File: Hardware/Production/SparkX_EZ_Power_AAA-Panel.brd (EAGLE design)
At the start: 187.2 x 136.7 mm, 1386 parts, among them J10 AVR_SPI_PROG_3X2TESTPOINTS, J12 AVR_SPI_PROG_3X2TESTPOINTS, J14 AVR_SPI_PROG_3X2TESTPOINTS, J16 AVR_SPI_PROG_3X2TESTPOINTS, J18 AVR_SPI_PROG_3X2TESTPOINTS, J20 AVR_SPI_PROG_3X2TESTPOINTS, J22 AVR_SPI_PROG_3X2TESTPOINTS, J24 AVR_SPI_PROG_3X2TESTPOINTS, J26 AVR_SPI_PROG_3X2TESTPOINTS, J28 AVR_SPI_PROG_3X2TESTPOINTS, J3 AVR_SPI_PROG_3X2TESTPOINTS, J30 AVR_SPI_PROG_3X2TESTPOINTS, J32 AVR_SPI_PROG_3X2TESTPOINTS, J34 AVR_SPI_PROG_3X2TESTPOINTS, J36 AVR_SPI_PROG_3X2TESTPOINTS, J38 AVR_SPI_PROG_3X2TESTPOINTS, J4 AVR_SPI_PROG_3X2TESTPOINTS, J40 AVR_SPI_PROG_3X2TESTPOINTS, J42 AVR_SPI_PROG_3X2TESTPOINTS, J44 AVR_SPI_PROG_3X2TESTPOINTS, J46 AVR_SPI_PROG_3X2TESTPOINTS, J48 AVR_SPI_PROG_3X2TESTPOINTS, J50 AVR_SPI_PROG_3X2TESTPOINTS, J52 AVR_SPI_PROG_3X2TESTPOINTS, J54 AVR_SPI_PROG_3X2TESTPOINTS, J56 AVR_SPI_PROG_3X2TESTPOINTS, J58 AVR_SPI_PROG_3X2TESTPOINTS, J6 AVR_SPI_PROG_3X2TESTPOINTS, J60 AVR_SPI_PROG_3X2TESTPOINTS, J8 AVR_SPI_PROG_3X2TESTPOINTS, U1 ATTINY43_QFN20, U10 TPS61200, U11 ATTINY43_QFN20, U12 TPS61200, U13 ATTINY43_QFN20, U14 TPS61200, U15 ATTINY43_QFN20, U16 TPS61200, U17 ATTINY43_QFN20, U18 TPS61200, U19 ATTINY43_QFN20, U2 TPS61200, U20 TPS61200, U21 ATTINY43_QFN20, U22 TPS61200, U23 ATTINY43_QFN20, U24 TPS61200, U25 ATTINY43_QFN20, U26 TPS61200, U27 ATTINY43_QFN20, U28 TPS61200, U29 ATTINY43_QFN20, U3 ATTINY43_QFN20, U30 TPS61200, U31 ATTINY43_QFN20, U32 TPS61200, U33 ATTINY43_QFN20, U34 TPS61200, U35 ATTINY43_QFN20, U36 TPS61200, U37 ATTINY43_QFN20, U38 TPS61200, U39 ATTINY43_QFN20, U4 TPS61200, U40 TPS61200, U41 ATTINY43_QFN20, U42 TPS61200, U43 ATTINY43_QFN20, U44 TPS61200, U45 ATTINY43_QFN20, U46 TPS61200, U47 ATTINY43_QFN20, U48 TPS61200, U49 ATTINY43_QFN20, U5 ATTINY43_QFN20, U50 TPS61200, U51 ATTINY43_QFN20, U52 TPS61200, U53 ATTINY43_QFN20, U54 TPS61200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

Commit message: Final tweaks
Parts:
- added U$391, U$405, U$419: (no value), output:5#5V0
- added U$392, U$406, U$420: (no value), output:MAX0
- added U$393, U$395, U$407, U$409: SPARKX-LOGO3, SparkX:SPARKX-SMALL
- added U$394, U$408: (no value), output:#OUT#0
- added U$396, U$410: (no value), output:#IN#0
- added U$397, U$411: (no value), output:#VIN#0
- added U$398, U$412: (no value), output:#3V3_EN#0
- added U$399, U$413: (no value), output:#PROC_PWR#0
- added U$400, U$414: (no value), output:#AT_VCC#0
- added U$401, U$402, U$415, U$416: (no value), output:EZ_POWER_AAA0
- added U$403, U$417: (no value), output:#TXD#0
- added U$404, U$418: (no value), output:#RXD#0
- U$10, U$195, U$377: device output:5#5V_MAX0 -> output:5#5V0
- U$100, U$114, U$282, U$296: device output:EZ_POWER_AAA0 -> output:#OUT#0
- U$101, U$113, U$127, U$269, U$283, U$295, U$309, U$87: value (none) -> SPARKX-LOGO3; device output:EZ_POWER_AAA0 -> SparkX:SPARKX-SMALL
- U$102, U$284: device output:#TXD#0 -> output:#IN#0
- U$103, U$285: device output:#RXD#0 -> output:#VIN#0
- U$104, U$286: device output:5#5V_MAX0 -> output:#3V3_EN#0
- U$105, U$133, U$287, U$315: value SPARKX-LOGO3 -> (none); device SparkX:SPARKX-SMALL -> output:#PROC_PWR#0
- U$106, U$288: device output:#OUT#0 -> output:#AT_VCC#0
- U$107, U$248, U$261, U$276, U$289, U$66, U$79, U$94: value SPARKX-LOGO3 -> (none); device SparkX:SPARKX-SMALL -> output:EZ_POWER_AAA0
- U$108, U$121, U$290, U$303: device output:#IN#0 -> output:EZ_POWER_AAA0
- U$109, U$291: device output:#VIN#0 -> output:#TXD#0
- U$11, U$196, U$224, U$378, U$42: value SPARKX-LOGO3 -> (none); device SparkX:SPARKX-SMALL -> output:MAX0
- U$110, U$292: device output:#3V3_EN#0 -> output:#RXD#0
- U$111, U$293: device output:#PROC_PWR#0 -> output:5#5V0
- U$112, U$294: device output:#AT_VCC#0 -> output:MAX0
- U$115, U$141, U$297, U$323: value (none) -> SPARKX-LOGO3; device output:#TXD#0 -> SparkX:SPARKX-SMALL
- U$116, U$298: device output:#RXD#0 -> output:#IN#0
- U$117, U$299: device output:5#5V_MAX0 -> output:#VIN#0
- U$118, U$146, U$300, U$328: value SPARKX-LOGO3 -> (none); device SparkX:SPARKX-SMALL -> output:#3V3_EN#0
- U$119, U$301: device output:#OUT#0 -> output:#PROC_PWR#0
- U$120, U$274, U$302, U$92: value SPARKX-LOGO3 -> (none); device SparkX:SPARKX-SMALL -> output:#AT_VCC#0
- U$122, U$135, U$304, U$317: device output:#VIN#0 -> output:EZ_POWER_AAA0
- U$123, U$305: device output:#3V3_EN#0 -> output:#TXD#0
- U$124, U$306: device output:#PROC_PWR#0 -> output:#RXD#0
- U$125, U$307: device output:#AT_VCC#0 -> output:5#5V0
- U$126, U$140, U$308, U$322: device output:EZ_POWER_AAA0 -> output:MAX0
- U$128, U$310: device output:#TXD#0 -> output:#OUT#0
- U$129, U$155, U$311, U$337: value (none) -> SPARKX-LOGO3; device output:#RXD#0 -> SparkX:SPARKX-SMALL
- U$130, U$312: device output:5#5V_MAX0 -> output:#IN#0
- U$131, U$159, U$313, U$341: value SPARKX-LOGO3 -> (none); device SparkX:SPARKX-SMALL -> output:#VIN#0
- U$132, U$314: device output:#OUT#0 -> output:#3V3_EN#0
- U$134, U$316: device output:#IN#0 -> output:#AT_VCC#0
- U$136, U$149, U$318, U$331: device output:#3V3_EN#0 -> output:EZ_POWER_AAA0
- U$137, U$319: device output:#PROC_PWR#0 -> output:#TXD#0
- U$138, U$320: device output:#AT_VCC#0 -> output:#RXD#0
- U$139, U$153, U$321, U$335: device output:EZ_POWER_AAA0 -> output:5#5V0
- U$14, U$171, U$197, U$353, U$379: value (none) -> SPARKX-LOGO3; device output:#OUT#0 -> SparkX:SPARKX-SMALL
- U$142, U$324: device output:#RXD#0 -> output:#OUT#0
- U$143, U$169, U$325, U$351: value (none) -> SPARKX-LOGO3; device output:5#5V_MAX0 -> SparkX:SPARKX-SMALL
- U$144, U$172, U$326, U$354: value SPARKX-LOGO3 -> (none); device SparkX:SPARKX-SMALL -> output:#IN#0
- U$145, U$327: device output:#OUT#0 -> output:#VIN#0
- U$147, U$329: device output:#IN#0 -> output:#PROC_PWR#0
- U$148, U$330: device output:#VIN#0 -> output:#AT_VCC#0
- U$15, U$170, U$198, U$352, U$380: value SPARKX-LOGO3 -> (none); device SparkX:SPARKX-SMALL -> output:#OUT#0
- U$150, U$163, U$332, U$345: device output:#PROC_PWR#0 -> output:EZ_POWER_AAA0
- U$151, U$333: device output:#AT_VCC#0 -> output:#TXD#0
- U$152, U$166, U$334, U$348: device output:EZ_POWER_AAA0 -> output:#RXD#0
- U$154, U$336: device output:#TXD#0 -> output:MAX0
- U$156, U$338: device output:5#5V_MAX0 -> output:#OUT#0
- U$158, U$340: device output:#OUT#0 -> output:#IN#0
- U$16, U$199, U$225, U$381, U$43: value (none) -> SPARKX-LOGO3; device output:#IN#0 -> SparkX:SPARKX-SMALL
- U$160, U$342: device output:#IN#0 -> output:#3V3_EN#0
- U$161, U$343: device output:#VIN#0 -> output:#PROC_PWR#0
- U$162, U$344: device output:#3V3_EN#0 -> output:#AT_VCC#0
- U$164, U$177, U$346, U$359: device output:#AT_VCC#0 -> output:EZ_POWER_AAA0
- U$165, U$179, U$347, U$361: device output:EZ_POWER_AAA0 -> output:#TXD#0
- U$167, U$349: device output:#TXD#0 -> output:5#5V0
- U$168, U$350: device output:#RXD#0 -> output:MAX0
- U$17, U$200, U$382: device output:#VIN#0 -> output:#IN#0
- U$173, U$355: device output:#IN#0 -> output:#VIN#0
- U$174, U$356: device output:#VIN#0 -> output:#3V3_EN#0
- U$175, U$357: device output:#3V3_EN#0 -> output:#PROC_PWR#0
- U$176, U$358: device output:#PROC_PWR#0 -> output:#AT_VCC#0
- U$18, U$201, U$383: device output:#3V3_EN#0 -> output:#VIN#0
- U$180, U$362: device output:#TXD#0 -> output:#RXD#0
- U$181, U$363: device output:#RXD#0 -> output:5#5V0
- U$182, U$364: device output:5#5V_MAX0 -> output:MAX0
- U$19, U$202, U$384: device output:#PROC_PWR#0 -> output:#3V3_EN#0
- U$203, U$21, U$385: device output:#AT_VCC#0 -> output:#PROC_PWR#0
- U$204, U$218, U$22, U$36, U$386: device output:EZ_POWER_AAA0 -> output:#AT_VCC#0
- U$206, U$219, U$24, U$37, U$388: device output:#TXD#0 -> output:EZ_POWER_AAA0
- U$207, U$25, U$389: device output:#RXD#0 -> output:#TXD#0
- U$208, U$26, U$390: device output:5#5V_MAX0 -> output:#RXD#0
- U$209, U$237, U$27, U$55: value SPARKX-LOGO3 -> (none); device SparkX:SPARKX-SMALL -> output:5#5V0
- U$210, U$28: device output:#OUT#0 -> output:MAX0
- U$212, U$30: device output:#IN#0 -> output:#OUT#0
- U$213, U$239, U$31, U$57: value (none) -> SPARKX-LOGO3; device output:#VIN#0 -> SparkX:SPARKX-SMALL
- U$214, U$32: device output:#3V3_EN#0 -> output:#IN#0
- U$215, U$33: device output:#PROC_PWR#0 -> output:#VIN#0
- U$216, U$34: device output:#AT_VCC#0 -> output:#3V3_EN#0
- U$217, U$231, U$35, U$49: device output:EZ_POWER_AAA0 -> output:#PROC_PWR#0
- U$220, U$233, U$38, U$51: device output:#RXD#0 -> output:EZ_POWER_AAA0
- U$221, U$39: device output:5#5V_MAX0 -> output:#TXD#0
- U$222, U$250, U$40, U$68: value SPARKX-LOGO3 -> (none); device SparkX:SPARKX-SMALL -> output:#RXD#0
- U$223, U$41: device output:#OUT#0 -> output:5#5V0
- U$226, U$44: device output:#VIN#0 -> output:#OUT#0
- U$227, U$253, U$45, U$71: value (none) -> SPARKX-LOGO3; device output:#3V3_EN#0 -> SparkX:SPARKX-SMALL
- U$228, U$46: device output:#PROC_PWR#0 -> output:#IN#0
- U$229, U$47: device output:#AT_VCC#0 -> output:#VIN#0
- U$230, U$244, U$48, U$62: device output:EZ_POWER_AAA0 -> output:#3V3_EN#0
- U$232, U$50: device output:#TXD#0 -> output:#AT_VCC#0
- U$234, U$247, U$52, U$65: device output:5#5V_MAX0 -> output:EZ_POWER_AAA0
- U$235, U$263, U$53, U$81: value SPARKX-LOGO3 -> (none); device SparkX:SPARKX-SMALL -> output:#TXD#0
- U$236, U$54: device output:#OUT#0 -> output:#RXD#0
- U$238, U$56: device output:#IN#0 -> output:MAX0
- U$240, U$58: device output:#3V3_EN#0 -> output:#OUT#0
- U$241, U$267, U$59, U$85: value (none) -> SPARKX-LOGO3; device output:#PROC_PWR#0 -> SparkX:SPARKX-SMALL
- U$242, U$60: device output:#AT_VCC#0 -> output:#IN#0
- U$243, U$257, U$61, U$75: device output:EZ_POWER_AAA0 -> output:#VIN#0
- U$245, U$63: device output:#TXD#0 -> output:#PROC_PWR#0
- U$246, U$64: device output:#RXD#0 -> output:#AT_VCC#0
- U$249, U$67: device output:#OUT#0 -> output:#TXD#0
- U$251, U$69: device output:#IN#0 -> output:5#5V0
- U$252, U$70: device output:#VIN#0 -> output:MAX0
- U$254, U$72: device output:#PROC_PWR#0 -> output:#OUT#0
- U$255, U$281, U$73, U$99: value (none) -> SPARKX-LOGO3; device output:#AT_VCC#0 -> SparkX:SPARKX-SMALL
- U$256, U$270, U$74, U$88: device output:EZ_POWER_AAA0 -> output:#IN#0
- U$258, U$76: device output:#TXD#0 -> output:#3V3_EN#0
- U$259, U$77: device output:#RXD#0 -> output:#PROC_PWR#0
- U$260, U$78: device output:5#5V_MAX0 -> output:#AT_VCC#0
- U$262, U$275, U$80, U$93: device output:#OUT#0 -> output:EZ_POWER_AAA0
- U$264, U$82: device output:#IN#0 -> output:#RXD#0
- U$265, U$83: device output:#VIN#0 -> output:5#5V0
- U$266, U$84: device output:#3V3_EN#0 -> output:MAX0
- U$268, U$86: device output:#AT_VCC#0 -> output:#OUT#0
- U$271, U$89: device output:#TXD#0 -> output:#VIN#0
- U$272, U$90: device output:#RXD#0 -> output:#3V3_EN#0
- U$273, U$91: device output:5#5V_MAX0 -> output:#PROC_PWR#0
- U$277, U$95: device output:#IN#0 -> output:#TXD#0
- U$278, U$96: device output:#VIN#0 -> output:#RXD#0
- U$279, U$97: device output:#3V3_EN#0 -> output:5#5V0
- U$280, U$98: device output:#PROC_PWR#0 -> output:MAX0
- moved U$271 161.0 mm to (151.7, 51.3)
- moved U$133 159.4 mm to (150.7, 3.75)
- moved U$131 158.6 mm to (151.7, 10.2), flipped to the bottom
- moved U$273 157.8 mm to (150.7, 44.9), flipped to the bottom, turned to 0 degrees
- moved U$272 157.6 mm to (150.7, 55.1)
- moved U$268 156.8 mm to (151.6, 46.0)
- moved U$134 156.5 mm to (151.6, 20.3), flipped to the top
- moved U$267 155.7 mm to (155.8, 49.8), flipped to the top, turned to 90 degrees
- moved U$140 154.6 mm to (155.3, 29.5), flipped to the top
- moved U$136 150.1 mm to (151.6, 26.0)
- moved U$270 149.8 mm to (151.6, 75.9)
- moved U$132 148.8 mm to (150.7, 14.0), flipped to the bottom
- moved U$138 148.2 mm to (150.3, 30.5), flipped to the bottom
- moved U$139 146.9 mm to (155.3, 30.4), turned to 0 degrees
- moved U$135 146.3 mm to (147.8, 17.5), flipped to the top, turned to 90 degrees
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
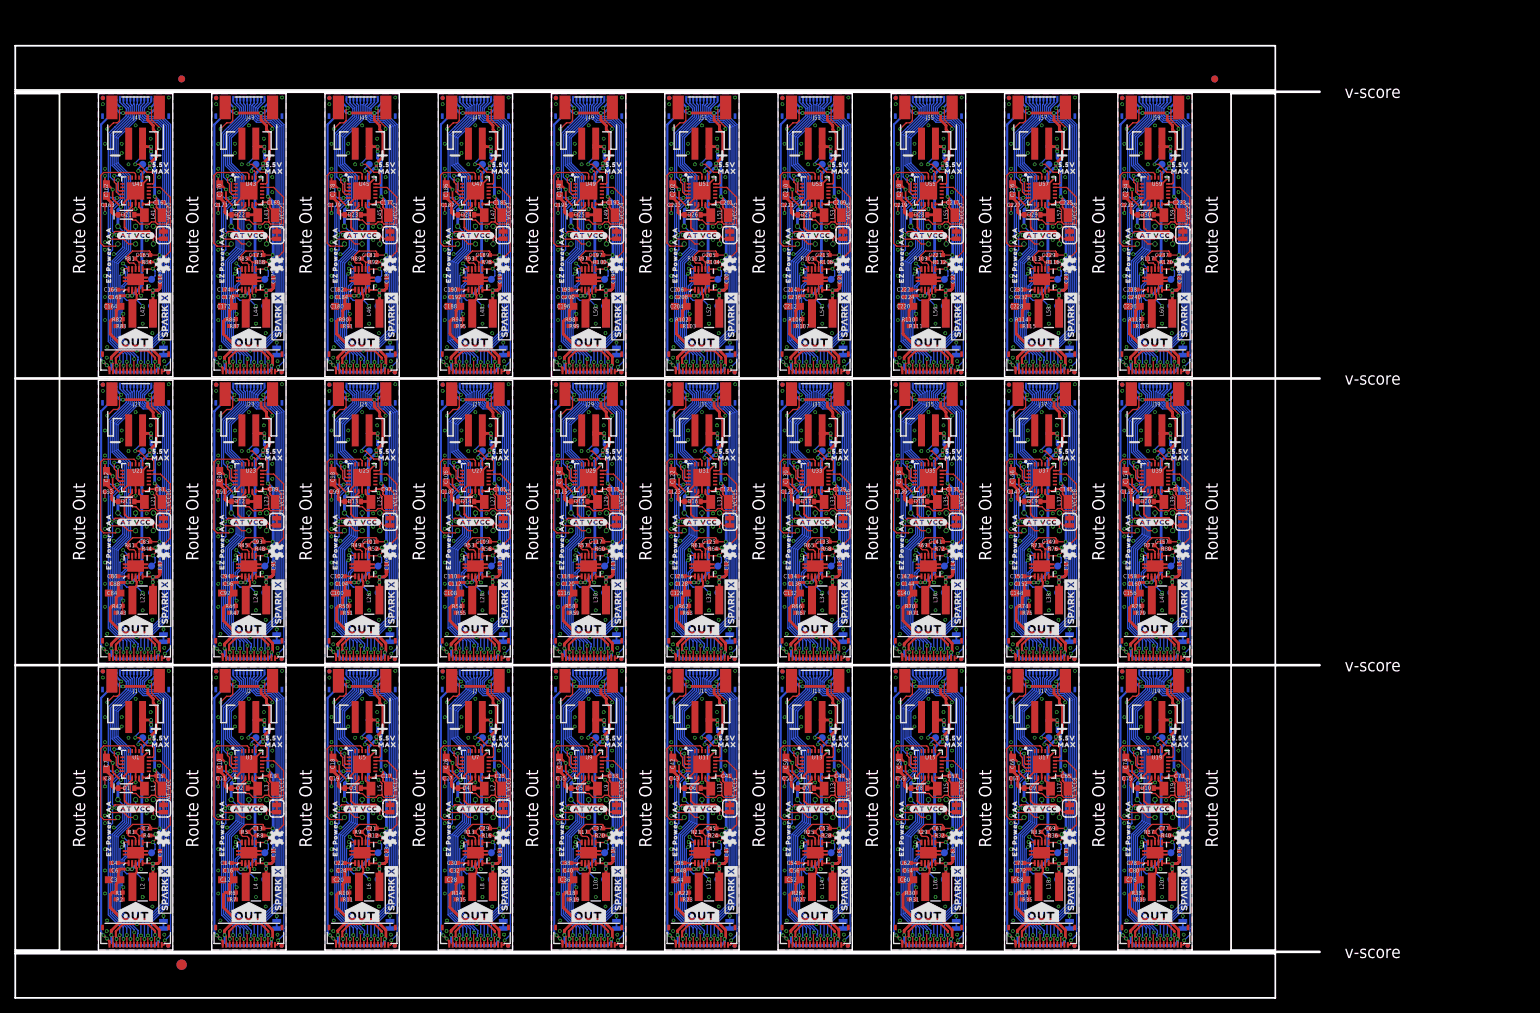
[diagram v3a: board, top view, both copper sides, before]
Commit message: Gapless production panel
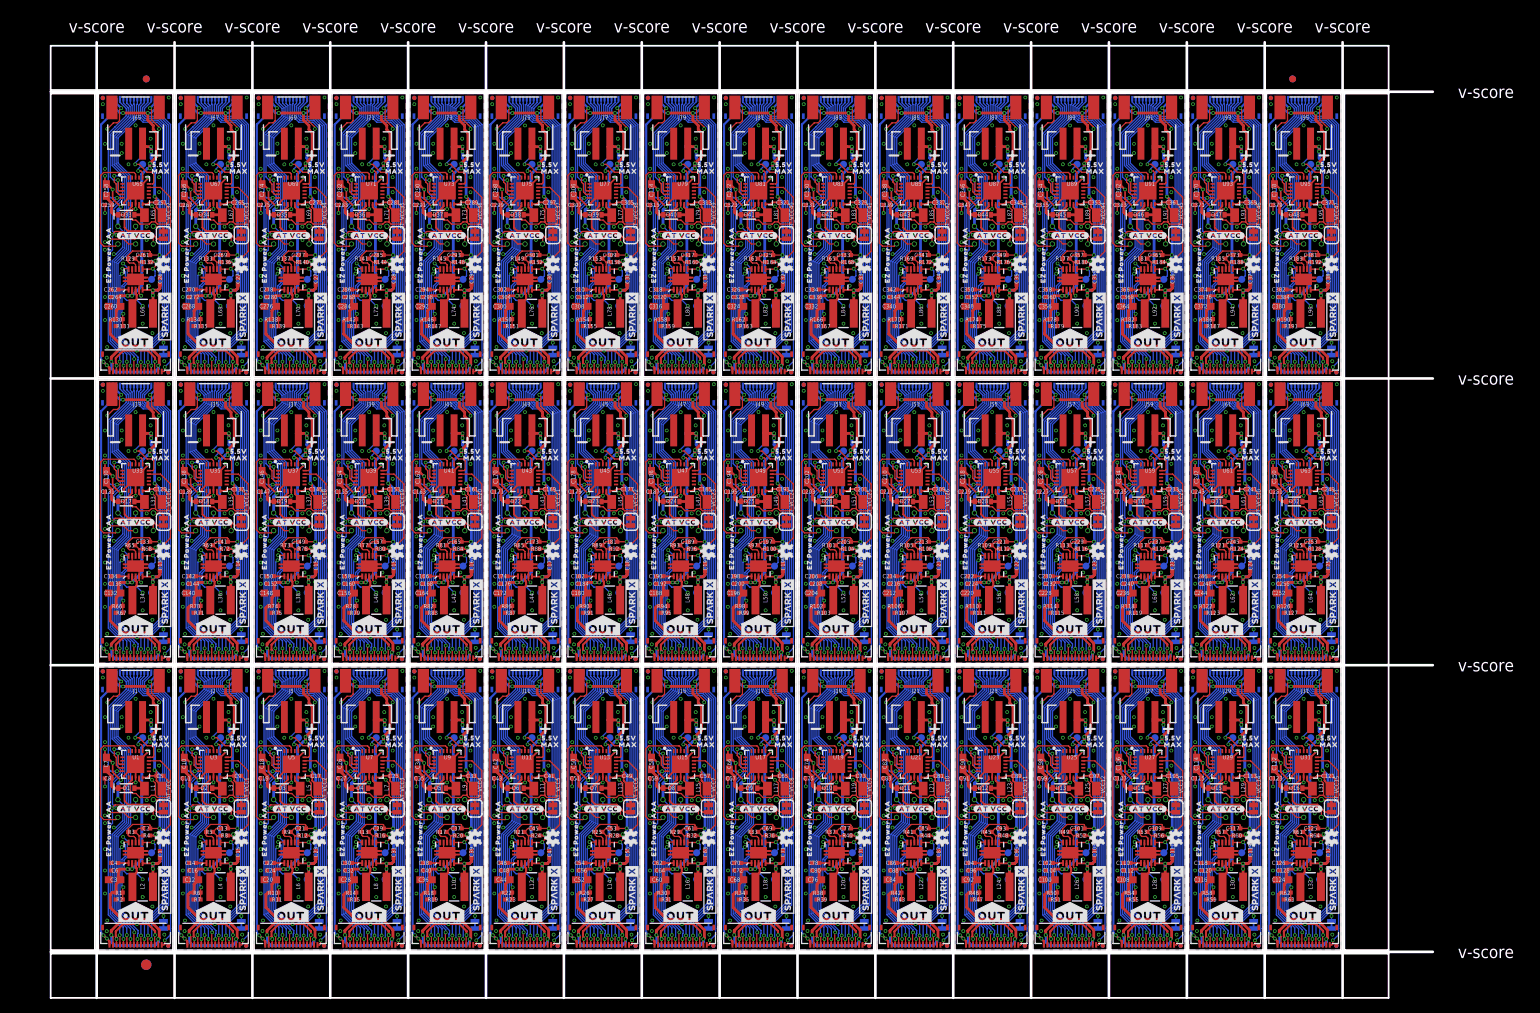
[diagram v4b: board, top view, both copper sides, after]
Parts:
- added 3V3_EN30, 3V3_EN31, 3V3_EN32, 3V3_EN33, 3V3_EN34, 3V3_EN35, 3V3_EN36, 3V3_EN37, 3V3_EN38, 3V3_EN39, 3V3_EN40, 3V3_EN41, 3V3_EN42, 3V3_EN43, 3V3_EN44, 3V3_EN45, 3V3_EN46, 3V3_EN47, RXD30, RXD31, RXD32, RXD33, RXD34, RXD35, RXD36, RXD37, RXD38, RXD39, RXD40, RXD41, RXD42, RXD43, RXD44, RXD45, RXD46, RXD47, TXD30, TXD31, TXD32, TXD33, TXD34, TXD35, TXD36, TXD37, TXD38, TXD39, TXD40, TXD41, TXD42, TXD43, TXD44, TXD45, TXD46, TXD47, VIN30, VIN31, VIN32, VIN33, VIN34, VIN35, VIN36, VIN37, VIN38, VIN39, VIN40, VIN41, VIN42, VIN43, VIN44, VIN45, VIN46, VIN47: TEST-POINT3X4, SparkFun-Connectors:PAD.03X.04
- added AT_VCC30, AT_VCC31, AT_VCC32, AT_VCC33, AT_VCC34, AT_VCC35, AT_VCC36, AT_VCC37, AT_VCC38, AT_VCC39, AT_VCC40, AT_VCC41, AT_VCC42, AT_VCC43, AT_VCC44, AT_VCC45, AT_VCC46, AT_VCC47, PROC_PWR_EN30, PROC_PWR_EN31, PROC_PWR_EN32, PROC_PWR_EN33, PROC_PWR_EN34, PROC_PWR_EN35, PROC_PWR_EN36, PROC_PWR_EN37, PROC_PWR_EN38, PROC_PWR_EN39, PROC_PWR_EN40, PROC_PWR_EN41, PROC_PWR_EN42, PROC_PWR_EN43, PROC_PWR_EN44, PROC_PWR_EN45, PROC_PWR_EN46, PROC_PWR_EN47: JUMPER-SMT_2_NC_TRACE_SILK, SparkFun-Jumpers:SMT-JUMPER_2_NC_TRACE_SILK
- added C241, C249, C257, C265, C273, C281, C289, C297, C305, C313, C321, C329, C337, C345, C353, C361, C369, C377: 4.7uF, SparkFun-Capacitors:0402-TIGHT
- added C242, C244, C250, C252, C258, C260, C266, C268, C274, C276, C282, C284, C290, C292, C298, C300, C306, C308, C314, C316, C322, C324, C330, C332, C338, C340, C346, C348, C354, C356, C362, C364, C370, C372, C378, C380: 22uF, SparkFun-Capacitors:0603
- added C243, C245, C246, C248, C251, C253, C254, C256, C259, C261, C262, C264, C267, C269, C270, C272, C275, C277, C278, C280, C283, C285, C286, C288, C291, C293, C294, C296, C299, C301, C302, C304, C307, C309, C310, C312, C315, C317, C318, C320, C323, C325, C326, C328, C331, C333, C334, C336, C339, C341, C342, C344, C347, C349, C350, C352, C355, C357, C358, C360, C363, C365, C366, C368, C371, C373, C374, C376, C379, C381, C382, C384: 0.1uF, SparkFun-Capacitors:0402-TIGHT
- added C247, C255, C263, C271, C279, C287, C295, C303, C311, C319, C327, C335, C343, C351, C359, C367, C375, C383: 10uF, SparkFun-Capacitors:0402-TIGHT
- added D31, D32, D33, D34, D35, D36, D37, D38, D39, D40, D41, D42, D43, D44, D45, D46, D47, D48: 1A/23V/620mV, SparkFun-DiscreteSemi:SOD-323
- added FD121, FD122, FD123, FD124, FD125, FD126, FD127, FD128, FD129, FD130, FD131, FD132, FD133, FD134, FD135, FD136, FD137, FD138, FD139, FD140, FD141, FD142, FD143, FD144, FD145, FD146, FD147, FD148, FD149, FD150, FD151, FD152, FD153, FD154, FD155, FD156, FD157, FD158, FD159, FD160, FD161, FD162, FD163, FD164, FD165, FD166, FD167, FD168, FD169, FD170, FD171, FD172, FD173, FD174, FD175, FD176, FD177, FD178, FD179, FD180, FD181, FD182, FD183, FD184, FD185, FD186, FD187, FD188, FD189, FD190, FD191, FD192: FIDUCIALUFIDUCIAL, SparkFun-Aesthetics:FIDUCIAL-MICRO
- added IN30, IN31, IN32, IN33, IN34, IN35, IN36, IN37, IN38, IN39, IN40, IN41, IN42, IN43, IN44, IN45, IN46, IN47, OUT30, OUT31, OUT32, OUT33, OUT34, OUT35, OUT36, OUT37, OUT38, OUT39, OUT40, OUT41, OUT42, OUT43, OUT44, OUT45, OUT46, OUT47: FPC_16_0.5MM_BACKFLIP, New_Parts_Connectors:FPC_16_DOUBLESIDED_BACKFLIP
- added J61, J63, J65, J67, J69, J71, J73, J75, J77, J79, J81, J83, J85, J87, J89, J91, J93, J95: (no value), SparkFun-Connectors:JST-2-SMD
- added J62, J64, J66, J68, J70, J72, J74, J76, J78, J80, J82, J84, J86, J88, J90, J92, J94, J96: AVR_SPI_PROG_3X2TESTPOINTS, SparkFun-Connectors:2X3_TEST_POINTS
- added L61, L63, L65, L67, L69, L71, L73, L75, L77, L79, L81, L83, L85, L87, L89, L91, L93, L95: 15uH, SparkFun-Coils:INDUCTOR_LQH32
- added L62, L64, L66, L68, L70, L72, L74, L76, L78, L80, L82, L84, L86, L88, L90, L92, L94, L96: 4.7μH, SparkFun-Coils:INDUCTOR_4X4MM
- added LOGO61, LOGO62, LOGO63, LOGO64, LOGO65, LOGO66, LOGO67, LOGO68, LOGO69, LOGO70, LOGO71, LOGO72, LOGO73, LOGO74, LOGO75, LOGO76, LOGO77, LOGO78, LOGO79, LOGO80, LOGO81, LOGO82, LOGO83, LOGO84, LOGO85, LOGO86, LOGO87, LOGO88, LOGO89, LOGO90, LOGO91, LOGO92, LOGO93, LOGO94, LOGO95, LOGO96: OSHW-LOGOMINI, SparkFun-Aesthetics:OSHW-LOGO-MINI
- added R121, R125, R129, R133, R137, R141, R145, R149, R153, R157, R161, R165, R169, R173, R177, R181, R185, R189: 453k, New-Parts_SparkFun-Resistors:0402-TIGHT
- added R122, R126, R130, R134, R138, R142, R146, R150, R154, R158, R162, R166, R170, R174, R178, R182, R186, R190: 1M, New-Parts_SparkFun-Resistors:0402-TIGHT
- added R123, R127, R131, R135, R139, R143, R147, R151, R155, R159, R163, R167, R171, R175, R179, R183, R187, R191: 180k, New-Parts_SparkFun-Resistors:0402-TIGHT
- added R124, R128, R132, R136, R140, R144, R148, R152, R156, R160, R164, R168, R172, R176, R180, R184, R188, R192: 150K, SparkFun-Resistors:0402-TIGHT
- added U$421, U$423, U$435, U$437, U$449, U$451, U$463, U$465, U$477, U$479, U$491, U$493, U$505, U$507, U$519, U$521, U$533, U$535, U$547, U$549, U$561, U$563, U$575, U$577, U$589, U$591, U$603, U$605, U$617, U$619, U$631, U$633, U$645, U$647, U$659, U$661: SPARKX-LOGO3, SparkX:SPARKX-SMALL
- added U$422, U$436, U$450, U$464, U$478, U$492, U$506, U$520, U$534, U$548, U$562, U$576, U$590, U$604, U$618, U$632, U$646, U$660: (no value), output:#OUT#0
- added U$424, U$438, U$452, U$466, U$480, U$494, U$508, U$522, U$536, U$550, U$564, U$578, U$592, U$606, U$620, U$634, U$648, U$662: (no value), output:#IN#0
- added U$425, U$439, U$453, U$467, U$481, U$495, U$509, U$523, U$537, U$551, U$565, U$579, U$593, U$607, U$621, U$635, U$649, U$663: (no value), output:#VIN#0
- added U$426, U$440, U$454, U$468, U$482, U$496, U$510, U$524, U$538, U$552, U$566, U$580, U$594, U$608, U$622, U$636, U$650, U$664: (no value), output:#3V3_EN#0
- added U$427, U$441, U$455, U$469, U$483, U$497, U$511, U$525, U$539, U$553, U$567, U$581, U$595, U$609, U$623, U$637, U$651, U$665: (no value), output:#PROC_PWR#0
- added U$428, U$442, U$456, U$470, U$484, U$498, U$512, U$526, U$540, U$554, U$568, U$582, U$596, U$610, U$624, U$638, U$652, U$666: (no value), output:#AT_VCC#0
- added U$429, U$430, U$443, U$444, U$457, U$458, U$471, U$472, U$485, U$486, U$499, U$500, U$513, U$514, U$527, U$528, U$541, U$542, U$555, U$556, U$569, U$570, U$583, U$584, U$597, U$598, U$611, U$612, U$625, U$626, U$639, U$640, U$653, U$654, U$667, U$668: (no value), output:EZ_POWER_AAA0
- added U$431, U$445, U$459, U$473, U$487, U$501, U$515, U$529, U$543, U$557, U$571, U$585, U$599, U$613, U$627, U$641, U$655, U$669: (no value), output:#TXD#0
- added U$432, U$446, U$460, U$474, U$488, U$502, U$516, U$530, U$544, U$558, U$572, U$586, U$600, U$614, U$628, U$642, U$656, U$670: (no value), output:#RXD#0
- added U$433, U$447, U$461, U$475, U$489, U$503, U$517, U$531, U$545, U$559, U$573, U$587, U$601, U$615, U$629, U$643, U$657, U$671: (no value), output:5#5V0
- added U$434, U$448, U$462, U$476, U$490, U$504, U$518, U$532, U$546, U$560, U$574, U$588, U$602, U$616, U$630, U$644, U$658, U$672: (no value), output:MAX0
- added U61, U63, U65, U67, U69, U71, U73, U75, U77, U79, U81, U83, U85, U87, U89, U91, U93, U95: ATTINY43_QFN20, SparkFun-IC-Microcontroller:QFN20_20M1
- added U62, U64, U66, U68, U70, U72, U74, U76, U78, U80, U82, U84, U86, U88, U90, U92, U94, U96: TPS61200, SparkFun-IC-Power:QFN-10_PAD
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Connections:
- new net !RESET!30: J62.5, U61.18
- new net !RESET!31: J64.5, U63.18
- new net !RESET!32: J66.5, U65.18
- new net !RESET!33: J68.5, U67.18
- new net !RESET!34: J70.5, U69.18
- new net !RESET!35: J72.5, U71.18
- new net !RESET!36: J74.5, U73.18
- new net !RESET!37: J76.5, U75.18
- new net !RESET!38: J78.5, U77.18
- new net !RESET!39: J80.5, U79.18
- new net !RESET!40: J82.5, U81.18
- new net !RESET!41: J84.5, U83.18
- new net !RESET!42: J86.5, U85.18
- new net !RESET!43: J88.5, U87.18
- new net !RESET!44: J90.5, U89.18
- new net !RESET!45: J92.5, U91.18
- new net !RESET!46: J94.5, U93.18
- new net !RESET!47: J96.5, U95.18
- new net 3.3V30: C244.1, C248.1, IN30.15, IN30.2, OUT30.15, OUT30.2, R122.2, U62.2
- new net 3.3V31: C252.1, C256.1, IN31.15, IN31.2, OUT31.15, OUT31.2, R126.2, U64.2
- new net 3.3V32: C260.1, C264.1, IN32.15, IN32.2, OUT32.15, OUT32.2, R130.2, U66.2
- new net 3.3V33: C268.1, C272.1, IN33.15, IN33.2, OUT33.15, OUT33.2, R134.2, U68.2
- new net 3.3V34: C276.1, C280.1, IN34.15, IN34.2, OUT34.15, OUT34.2, R138.2, U70.2
- new net 3.3V35: C284.1, C288.1, IN35.15, IN35.2, OUT35.15, OUT35.2, R142.2, U72.2
- new net 3.3V36: C292.1, C296.1, IN36.15, IN36.2, OUT36.15, OUT36.2, R146.2, U74.2
- new net 3.3V37: C300.1, C304.1, IN37.15, IN37.2, OUT37.15, OUT37.2, R150.2, U76.2
- new net 3.3V38: C308.1, C312.1, IN38.15, IN38.2, OUT38.15, OUT38.2, R154.2, U78.2
- new net 3.3V39: C316.1, C320.1, IN39.15, IN39.2, OUT39.15, OUT39.2, R158.2, U80.2
- new net 3.3V40: C324.1, C328.1, IN40.15, IN40.2, OUT40.15, OUT40.2, R162.2, U82.2
- new net 3.3V41: C332.1, C336.1, IN41.15, IN41.2, OUT41.15, OUT41.2, R166.2, U84.2
- new net 3.3V42: C340.1, C344.1, IN42.15, IN42.2, OUT42.15, OUT42.2, R170.2, U86.2
- new net 3.3V43: C348.1, C352.1, IN43.15, IN43.2, OUT43.15, OUT43.2, R174.2, U88.2
- new net 3.3V44: C356.1, C360.1, IN44.15, IN44.2, OUT44.15, OUT44.2, R178.2, U90.2
- new net 3.3V45: C364.1, C368.1, IN45.15, IN45.2, OUT45.15, OUT45.2, R182.2, U92.2
- new net 3.3V46: C372.1, C376.1, IN46.15, IN46.2, OUT46.15, OUT46.2, R186.2, U94.2
- new net 3.3V47: C380.1, C384.1, IN47.15, IN47.2, OUT47.15, OUT47.2, R190.2, U96.2
- new net 3V3_EN30: 3V3_EN30.1, U61.14, U62.6
- new net 3V3_EN31: 3V3_EN31.1, U63.14, U64.6
- new net 3V3_EN32: 3V3_EN32.1, U65.14, U66.6
- new net 3V3_EN33: 3V3_EN33.1, U67.14, U68.6
- new net 3V3_EN34: 3V3_EN34.1, U69.14, U70.6
- new net 3V3_EN35: 3V3_EN35.1, U71.14, U72.6
- new net 3V3_EN36: 3V3_EN36.1, U73.14, U74.6
- new net 3V3_EN37: 3V3_EN37.1, U75.14, U76.6
- new net 3V3_EN38: 3V3_EN38.1, U77.14, U78.6
- new net 3V3_EN39: 3V3_EN39.1, U79.14, U80.6
- new net 3V3_EN40: 3V3_EN40.1, U81.14, U82.6
- new net 3V3_EN41: 3V3_EN41.1, U83.14, U84.6
- new net 3V3_EN42: 3V3_EN42.1, U85.14, U86.6
- new net 3V3_EN43: 3V3_EN43.1, U87.14, U88.6
- new net 3V3_EN44: 3V3_EN44.1, U89.14, U90.6
- new net 3V3_EN45: 3V3_EN45.1, U91.14, U92.6
- new net 3V3_EN46: 3V3_EN46.1, U93.14, U94.6
- new net 3V3_EN47: 3V3_EN47.1, U95.14, U96.6
- new net AT_CIPO30: J62.1, U61.4
- new net AT_CIPO31: J64.1, U63.4
- new net AT_CIPO32: J66.1, U65.4
- new net AT_CIPO33: J68.1, U67.4
- new net AT_CIPO34: J70.1, U69.4
- new net AT_CIPO35: J72.1, U71.4
- new net AT_CIPO36: J74.1, U73.4
- new net AT_CIPO37: J76.1, U75.4
- new net AT_CIPO38: J78.1, U77.4
- new net AT_CIPO39: J80.1, U79.4
- new net AT_CIPO40: J82.1, U81.4
- new net AT_CIPO41: J84.1, U83.4
- new net AT_CIPO42: J86.1, U85.4
- new net AT_CIPO43: J88.1, U87.4
- new net AT_CIPO44: J90.1, U89.4
- new net AT_CIPO45: J92.1, U91.4
- new net AT_CIPO46: J94.1, U93.4
- new net AT_CIPO47: J96.1, U95.4
- new net AT_VCC30: AT_VCC30.2, C242.1, C243.1, D31.C, U61.7
- new net AT_VCC31: AT_VCC31.2, C250.1, C251.1, D32.C, U63.7
- new net AT_VCC32: AT_VCC32.2, C258.1, C259.1, D33.C, U65.7
- new net AT_VCC33: AT_VCC33.2, C266.1, C267.1, D34.C, U67.7
- new net AT_VCC34: AT_VCC34.2, C274.1, C275.1, D35.C, U69.7
- new net AT_VCC35: AT_VCC35.2, C282.1, C283.1, D36.C, U71.7
- new net AT_VCC36: AT_VCC36.2, C290.1, C291.1, D37.C, U73.7
- new net AT_VCC37: AT_VCC37.2, C298.1, C299.1, D38.C, U75.7
- new net AT_VCC38: AT_VCC38.2, C306.1, C307.1, D39.C, U77.7
- new net AT_VCC39: AT_VCC39.2, C314.1, C315.1, D40.C, U79.7
- new net AT_VCC40: AT_VCC40.2, C322.1, C323.1, D41.C, U81.7
- new net AT_VCC41: AT_VCC41.2, C330.1, C331.1, D42.C, U83.7
- new net AT_VCC42: AT_VCC42.2, C338.1, C339.1, D43.C, U85.7
- new net AT_VCC43: AT_VCC43.2, C346.1, C347.1, D44.C, U87.7
- new net AT_VCC44: AT_VCC44.2, C354.1, C355.1, D45.C, U89.7
- new net AT_VCC45: AT_VCC45.2, C362.1, C363.1, D46.C, U91.7
- new net AT_VCC46: AT_VCC46.2, C370.1, C371.1, D47.C, U93.7
- new net AT_VCC47: AT_VCC47.2, C378.1, C379.1, D48.C, U95.7
- new net CIPO30: IN30.6, OUT30.6
- new net CIPO31: IN31.6, OUT31.6
- new net CIPO32: IN32.6, OUT32.6
- new net CIPO33: IN33.6, OUT33.6
- new net CIPO34: IN34.6, OUT34.6
- new net CIPO35: IN35.6, OUT35.6
- new net CIPO36: IN36.6, OUT36.6
- new net CIPO37: IN37.6, OUT37.6
- new net CIPO38: IN38.6, OUT38.6
- new net CIPO39: IN39.6, OUT39.6
- new net CIPO40: IN40.6, OUT40.6
- new net CIPO41: IN41.6, OUT41.6
- new net CIPO42: IN42.6, OUT42.6
- new net CIPO43: IN43.6, OUT43.6
- new net CIPO44: IN44.6, OUT44.6
- new net CIPO45: IN45.6, OUT45.6
- new net CIPO46: IN46.6, OUT46.6
- new net CIPO47: IN47.6, OUT47.6
- new net COPI30: IN30.5, OUT30.5
- new net COPI31: IN31.5, OUT31.5
- new net COPI32: IN32.5, OUT32.5
- new net COPI33: IN33.5, OUT33.5
- new net COPI34: IN34.5, OUT34.5
- new net COPI35: IN35.5, OUT35.5
- new net COPI36: IN36.5, OUT36.5
- new net COPI37: IN37.5, OUT37.5
- new net COPI38: IN38.5, OUT38.5
- new net COPI39: IN39.5, OUT39.5
- new net COPI40: IN40.5, OUT40.5
- new net COPI41: IN41.5, OUT41.5
- new net COPI42: IN42.5, OUT42.5
- new net COPI43: IN43.5, OUT43.5
- new net COPI44: IN44.5, OUT44.5
- new net COPI45: IN45.5, OUT45.5
- new net COPI46: IN46.5, OUT46.5
- new net COPI47: IN47.5, OUT47.5
- new net CS100: IN33.8, OUT33.8
- new net CS101: IN33.9, OUT33.9
- new net CS102: IN34.7, OUT34.7
- new net CS103: IN34.8, OUT34.8
- new net CS104: IN34.9, OUT34.9
- new net CS105: IN35.7, OUT35.7
- new net CS106: IN35.8, OUT35.8
- new net CS107: IN35.9, OUT35.9
- new net CS108: IN36.7, OUT36.7
- new net CS109: IN36.8, OUT36.8
- new net CS110: IN36.9, OUT36.9
- new net CS111: IN37.7, OUT37.7
- new net CS112: IN37.8, OUT37.8
- new net CS113: IN37.9, OUT37.9
- new net CS114: IN38.7, OUT38.7
- new net CS115: IN38.8, OUT38.8
- new net CS116: IN38.9, OUT38.9
- new net CS117: IN39.7, OUT39.7
- new net CS118: IN39.8, OUT39.8
- new net CS119: IN39.9, OUT39.9
- new net CS120: IN40.7, OUT40.7
- new net CS121: IN40.8, OUT40.8
- new net CS122: IN40.9, OUT40.9
- new net CS123: IN41.7, OUT41.7
- new net CS124: IN41.8, OUT41.8
- new net CS125: IN41.9, OUT41.9
- new net CS126: IN42.7, OUT42.7
- new net CS127: IN42.8, OUT42.8
- new net CS128: IN42.9, OUT42.9
- new net CS129: IN43.7, OUT43.7
- new net CS130: IN43.8, OUT43.8
- new net CS131: IN43.9, OUT43.9
- new net CS132: IN44.7, OUT44.7
- new net CS133: IN44.8, OUT44.8
- new net CS134: IN44.9, OUT44.9
- new net CS135: IN45.7, OUT45.7
- new net CS136: IN45.8, OUT45.8
- new net CS137: IN45.9, OUT45.9
- new net CS138: IN46.7, OUT46.7
- new net CS139: IN46.8, OUT46.8
- new net CS140: IN46.9, OUT46.9
- new net CS141: IN47.7, OUT47.7
- new net CS142: IN47.8, OUT47.8
- new net CS143: IN47.9, OUT47.9
- new net CS90: IN30.7, OUT30.7
- new net CS91: IN30.8, OUT30.8
- new net CS92: IN30.9, OUT30.9
- new net CS93: IN31.7, OUT31.7
- new net CS94: IN31.8, OUT31.8
- new net CS95: IN31.9, OUT31.9
- new net CS96: IN32.7, OUT32.7
- new net CS97: IN32.8, OUT32.8
- new net CS98: IN32.9, OUT32.9
- new net CS99: IN33.7, OUT33.7
- new net FB30: R122.1, R123.2, U62.10
- new net FB31: R126.1, R127.2, U64.10
- new net FB32: R130.1, R131.2, U66.10
- new net FB33: R134.1, R135.2, U68.10
- new net FB34: R138.1, R139.2, U70.10
- new net FB35: R142.1, R143.2, U72.10
- new net FB36: R146.1, R147.2, U74.10
- new net FB37: R150.1, R151.2, U76.10
- new net FB38: R154.1, R155.2, U78.10
- new net FB39: R158.1, R159.2, U80.10
- new net FB40: R162.1, R163.2, U82.10
- new net FB41: R166.1, R167.2, U84.10
- new net FB42: R170.1, R171.2, U86.10
- new net FB43: R174.1, R175.2, U88.10
- new net FB44: R178.1, R179.2, U90.10
- new net FB45: R182.1, R183.2, U92.10
- new net FB46: R186.1, R187.2, U94.10
- new net FB47: R190.1, R191.2, U96.10
- new net GND30: C241.2, C242.2, C243.2, C244.2, C246.2, C247.2, C248.2, IN30.14, IN30.3, J61.1, J62.6, OUT30.14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
- new net GND31: C249.2, C250.2, C251.2, C252.2, C254.2, C255.2, C256.2, IN31.14, IN31.3, J63.1, J64.6, OUT31.14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
- new net GND32: C257.2, C258.2, C259.2, C260.2, C262.2, C263.2, C264.2, IN32.14, IN32.3, J65.1, J66.6, OUT32.14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
- new net GND33: C265.2, C266.2, C267.2, C268.2, C270.2, C271.2, C272.2, IN33.14, IN33.3, J67.1, J68.6, OUT33.14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
- new net GND34: C273.2, C274.2, C275.2, C276.2, C278.2, C279.2, C280.2, IN34.14, IN34.3, J69.1, J70.6, OUT34.14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
- new net GND35: C281.2, C282.2, C283.2, C284.2, C286.2, C287.2, C288.2, IN35.14, IN35.3, J71.1, J72.6, OUT35.14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
- new net GND36: C289.2, C290.2, C291.2, C292.2, C294.2, C295.2, C296.2, IN36.14, IN36.3, J73.1, J74.6, OUT36.14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
- new net GND37: C297.2, C298.2, C299.2, C300.2, C302.2, C303.2, C304.2, IN37.14, IN37.3, J75.1, J76.6, OUT37.14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
- new net GND38: C305.2, C306.2, C307.2, C308.2, C310.2, C311.2, C312.2, IN38.14, IN38.3, J77.1, J78.6, OUT38.14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
- new net GND39: C313.2, C314.2, C315.2, C316.2, C318.2, C319.2, C320.2, IN39.14, IN39.3, J79.1, J80.6, OUT39.14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
- new net GND40: C321.2, C322.2, C323.2, C324.2, C326.2, C327.2, C328.2, IN40.14, IN40.3, J81.1, J82.6, OUT40.14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
- new net GND41: C329.2, C330.2, C331.2, C332.2, C334.2, C335.2, C336.2, IN41.14, IN41.3, J83.1, J84.6, OUT41.14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
- new net GND42: C337.2, C338.2, C339.2, C340.2, C342.2, C343.2, C344.2, IN42.14, IN42.3, J85.1, J86.6, OUT42.14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
- new net GND43: C345.2, C346.2, C347.2, C348.2, C350.2, C351.2, C352.2, IN43.14, IN43.3, J87.1, J88.6, OUT43.14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
- new net GND44: C353.2, C354.2, C355.2, C356.2, C358.2, C359.2, C360.2, IN44.14, IN44.3, J89.1, J90.6, OUT44.14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
- new net GND45: C361.2, C362.2, C363.2, C364.2, C366.2, C367.2, C368.2, IN45.14, IN45.3, J91.1, J92.6, OUT45.14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
- new net GND46: C369.2, C370.2, C371.2, C372.2, C374.2, C375.2, C376.2, IN46.14, IN46.3, J93.1, J94.6, OUT46.14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
- new net GND47: C377.2, C378.2, C379.2, C380.2, C382.2, C383.2, C384.2, IN47.14, IN47.3, J95.1, J96.6, OUT47.14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
- new net GPIO60: IN30.10, OUT30.10
- new net GPIO61: IN30.11, OUT30.11
- new net GPIO62: IN31.10, OUT31.10
- new net GPIO63: IN31.11, OUT31.11
- new net GPIO64: IN32.10, OUT32.10
- new net GPIO65: IN32.11, OUT32.11
- new net GPIO66: IN33.10, OUT33.10
- new net GPIO67: IN33.11, OUT33.11
- new net GPIO68: IN34.10, OUT34.10
- new net GPIO69: IN34.11, OUT34.11
- new net GPIO70: IN35.10, OUT35.10
- new net GPIO71: IN35.11, OUT35.11
- new net GPIO72: IN36.10, OUT36.10
- new net GPIO73: IN36.11, OUT36.11
- new net GPIO74: IN37.10, OUT37.10
- new net GPIO75: IN37.11, OUT37.11
- new net GPIO76: IN38.10, OUT38.10
- new net GPIO77: IN38.11, OUT38.11
- new net GPIO78: IN39.10, OUT39.10
- new net GPIO79: IN39.11, OUT39.11
- new net GPIO80: IN40.10, OUT40.10
- new net GPIO81: IN40.11, OUT40.11
- new net GPIO82: IN41.10, OUT41.10
- new net GPIO83: IN41.11, OUT41.11
- new net GPIO84: IN42.10, OUT42.10
- new net GPIO85: IN42.11, OUT42.11
- new net GPIO86: IN43.10, OUT43.10
- new net GPIO87: IN43.11, OUT43.11
- new net GPIO88: IN44.10, OUT44.10
- new net GPIO89: IN44.11, OUT44.11
- new net GPIO90: IN45.10, OUT45.10
- new net GPIO91: IN45.11, OUT45.11
- new net GPIO92: IN46.10, OUT46.10
- new net GPIO93: IN46.11, OUT46.11
- new net GPIO94: IN47.10, OUT47.10
- new net GPIO95: IN47.11, OUT47.11
- new net N$121: D31.A, L61.P$1, U61.9
- new net N$122: AT_VCC30.1, J62.2
- new net N$123: L62.P$1, U62.3
- new net N$124: C246.1, U62.1
- new net N$125: D32.A, L63.P$1, U63.9
- new net N$126: AT_VCC31.1, J64.2
- new net N$127: L64.P$1, U64.3
- new net N$128: C254.1, U64.1
- new net N$129: D33.A, L65.P$1, U65.9
- new net N$130: AT_VCC32.1, J66.2
- new net N$131: L66.P$1, U66.3
- new net N$132: C262.1, U66.1
- new net N$133: D34.A, L67.P$1, U67.9
- new net N$134: AT_VCC33.1, J68.2
- new net N$135: L68.P$1, U68.3
- new net N$136: C270.1, U68.1
- new net N$137: D35.A, L69.P$1, U69.9
- new net N$138: AT_VCC34.1, J70.2
- new net N$139: L70.P$1, U70.3
- new net N$140: C278.1, U70.1
- new net N$141: D36.A, L71.P$1, U71.9
- new net N$142: AT_VCC35.1, J72.2
- new net N$143: L72.P$1, U72.3
- new net N$144: C286.1, U72.1
- new net N$145: D37.A, L73.P$1, U73.9
- new net N$146: AT_VCC36.1, J74.2
- new net N$147: L74.P$1, U74.3
- new net N$148: C294.1, U74.1
- new net N$149: D38.A, L75.P$1, U75.9
- new net N$150: AT_VCC37.1, J76.2
- new net N$151: L76.P$1, U76.3
- new net N$152: C302.1, U76.1
- new net N$153: D39.A, L77.P$1, U77.9
- new net N$154: AT_VCC38.1, J78.2
- new net N$155: L78.P$1, U78.3
- new net N$156: C310.1, U78.1
- new net N$157: D40.A, L79.P$1, U79.9
- new net N$158: AT_VCC39.1, J80.2
- new net N$159: L80.P$1, U80.3
- new net N$160: C318.1, U80.1
- new net N$161: D41.A, L81.P$1, U81.9
- new net N$162: AT_VCC40.1, J82.2
- new net N$163: L82.P$1, U82.3
- new net N$164: C326.1, U82.1
- new net N$165: D42.A, L83.P$1, U83.9
- new net N$166: AT_VCC41.1, J84.2
- new net N$167: L84.P$1, U84.3
- new net N$168: C334.1, U84.1
- new net N$169: D43.A, L85.P$1, U85.9
- new net N$170: AT_VCC42.1, J86.2
- new net N$171: L86.P$1, U86.3
- new net N$172: C342.1, U86.1
- new net N$173: D44.A, L87.P$1, U87.9
- new net N$174: AT_VCC43.1, J88.2
- new net N$175: L88.P$1, U88.3
- new net N$176: C350.1, U88.1
- new net N$177: D45.A, L89.P$1, U89.9
- new net N$178: AT_VCC44.1, J90.2
- new net N$179: L90.P$1, U90.3
- new net N$180: C358.1, U90.1
- new net N$181: D46.A, L91.P$1, U91.9
- new net N$182: AT_VCC45.1, J92.2
- new net N$183: L92.P$1, U92.3
- new net N$184: C366.1, U92.1
- new net N$185: D47.A, L93.P$1, U93.9
- new net N$186: AT_VCC46.1, J94.2
- new net N$187: L94.P$1, U94.3
- new net N$188: C374.1, U94.1
- new net N$189: D48.A, L95.P$1, U95.9
- new net N$190: AT_VCC47.1, J96.2
- new net N$191: L96.P$1, U96.3
- new net N$192: C382.1, U96.1
- new net PROC_PWR_EN30: IN30.1, OUT30.1, PROC_PWR_EN30.1
- new net PROC_PWR_EN31: IN31.1, OUT31.1, PROC_PWR_EN31.1
- new net PROC_PWR_EN32: IN32.1, OUT32.1, PROC_PWR_EN32.1
- new net PROC_PWR_EN33: IN33.1, OUT33.1, PROC_PWR_EN33.1
- new net PROC_PWR_EN34: IN34.1, OUT34.1, PROC_PWR_EN34.1
- new net PROC_PWR_EN35: IN35.1, OUT35.1, PROC_PWR_EN35.1
- new net PROC_PWR_EN36: IN36.1, OUT36.1, PROC_PWR_EN36.1
- new net PROC_PWR_EN37: IN37.1, OUT37.1, PROC_PWR_EN37.1
- new net PROC_PWR_EN38: IN38.1, OUT38.1, PROC_PWR_EN38.1
- new net PROC_PWR_EN39: IN39.1, OUT39.1, PROC_PWR_EN39.1
- new net PROC_PWR_EN40: IN40.1, OUT40.1, PROC_PWR_EN40.1
- new net PROC_PWR_EN41: IN41.1, OUT41.1, PROC_PWR_EN41.1
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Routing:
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- added copper zone on layer 1, net GND30
- added copper zone on layer 16, net GND30
- added copper zone on layer 1, net GND31
- added copper zone on layer 16, net GND31
- added copper zone on layer 1, net GND32
- added copper zone on layer 16, net GND32
- added copper zone on layer 1, net GND33
- added copper zone on layer 16, net GND33
- added copper zone on layer 1, net GND34
- added copper zone on layer 16, net GND34
- added copper zone on layer 1, net GND35
- added copper zone on layer 16, net GND35
- added copper zone on layer 1, net GND36
- added copper zone on layer 16, net GND36
- added copper zone on layer 1, net GND37
- added copper zone on layer 16, net GND37
- added copper zone on layer 1, net GND38
- added copper zone on layer 16, net GND38
- added copper zone on layer 1, net GND39
- added copper zone on layer 16, net GND39
- added copper zone on layer 1, net GND40
- added copper zone on layer 16, net GND40
- added copper zone on layer 1, net GND41
- added copper zone on layer 16, net GND41
- added copper zone on layer 1, net GND42
- added copper zone on layer 16, net GND42
- added copper zone on layer 1, net GND43
- added copper zone on layer 16, net GND43
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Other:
- board size 187.2 x 136.7 mm -> 198.4 x 137.2 mm
- board text removed: "Route Out"
